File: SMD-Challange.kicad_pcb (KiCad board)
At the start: 2 copper layers, 40 x 40 mm, 22 parts, among them SW1 SW_DPDT_x2, U1 NE555, U2 4017

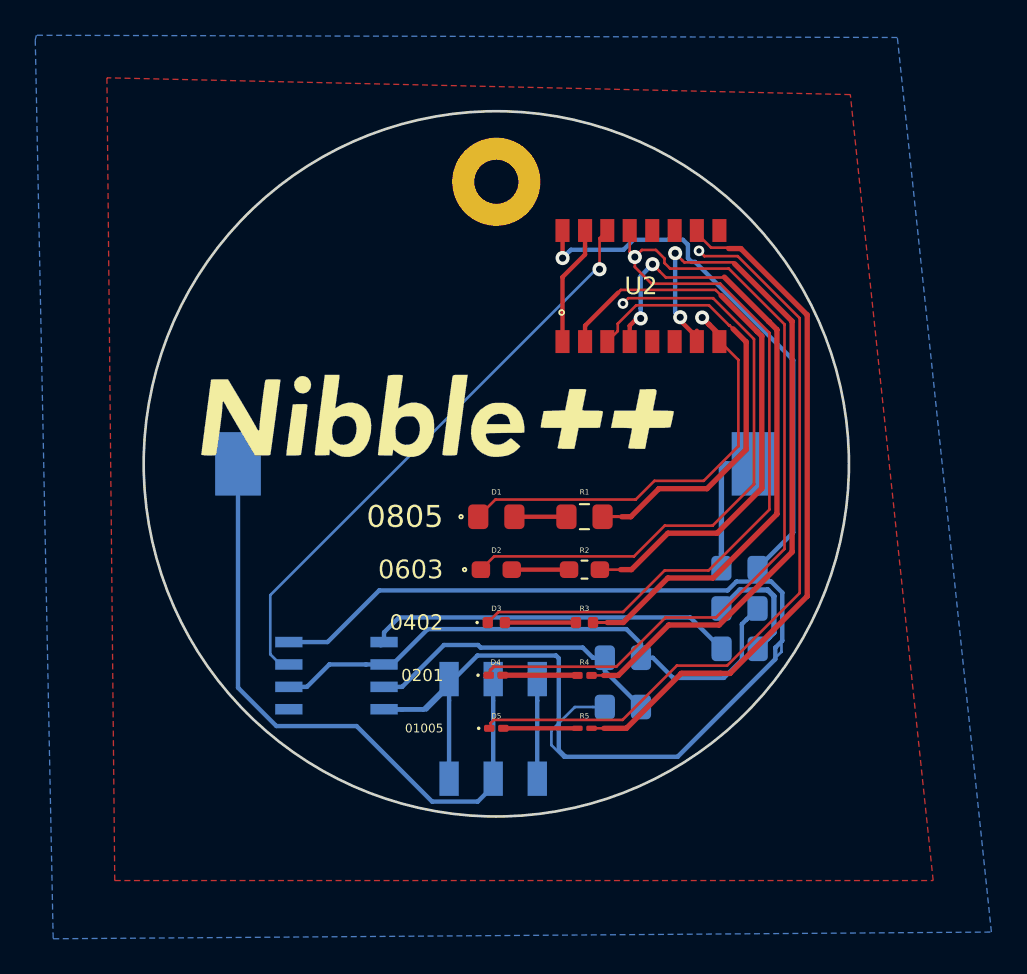
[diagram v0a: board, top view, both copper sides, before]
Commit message: remove some silkscreen features and cleanup layout
Signed-off-by: Thomas Schmid <tom@binary-kitchen.de>
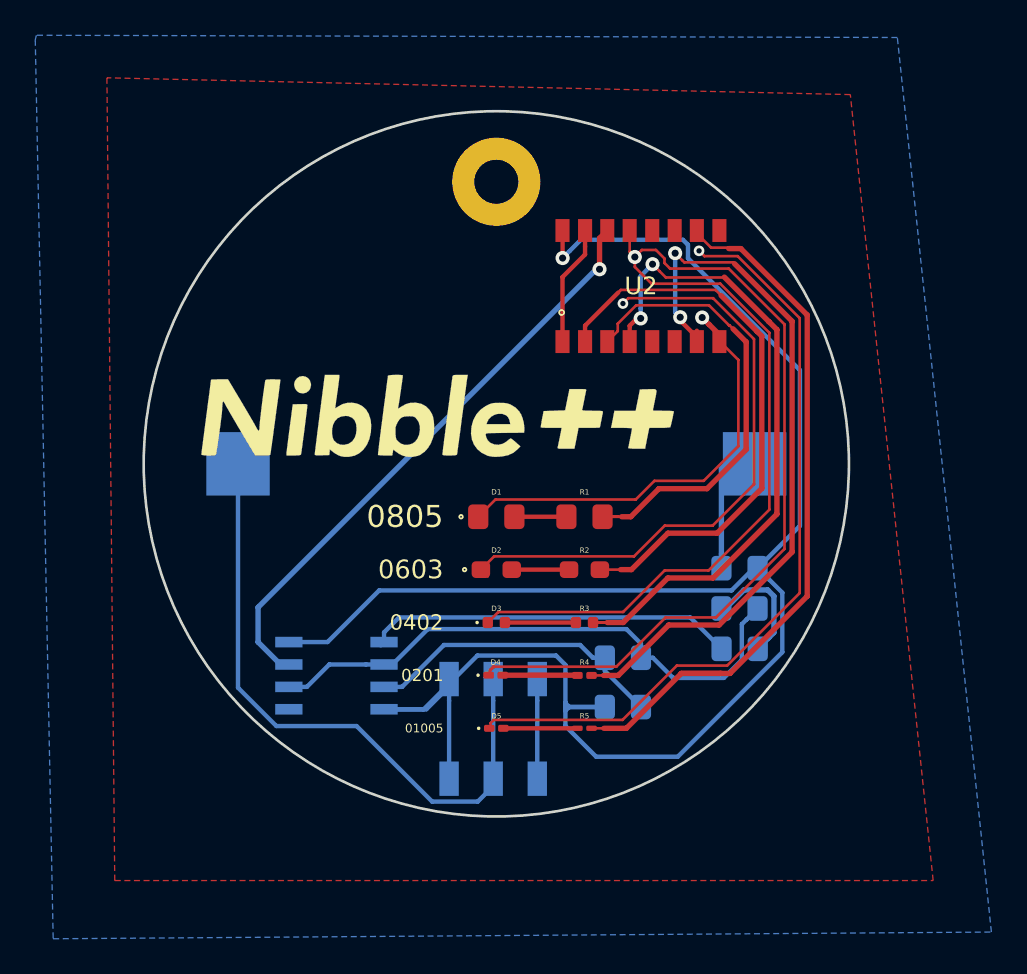
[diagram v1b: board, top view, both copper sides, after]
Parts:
- BT1: footprint Battery:BatteryHolder_Keystone_1060_1x2032 -> SMD-Challange:BatteryHolder_Keystone_1060_1x2032
- R1: footprint Resistor_SMD:R_0805_2012Metric_Pad1.15x1.40mm_HandSolder -> SMD-Challange:R_0805_2012Metric_Pad1.15x1.40mm_HandSolder
- R2: footprint Resistor_SMD:R_0603_1608Metric_Pad1.05x0.95mm_HandSolder -> SMD-Challange:R_0603_1608Metric_Pad1.05x0.95mm_HandSolder
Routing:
- net VS: track 131.6 -> 110.8 mm
- net Net-(U1-Pad3): track 33.4 -> 33.9 mm
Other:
- rule pad_to_mask_clearance: 0.051 -> 0.0508
- rule solder_mask_min_width: 0.25 -> 0.0508
